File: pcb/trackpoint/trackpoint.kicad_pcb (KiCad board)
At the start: 2 copper layers, 45 x 135.9 mm, 5 parts, among them SW1 SW_RESET, SW3 SW_RESET, U1 ProMicro, U2 trackpoint_R61, U3 mouse_wheel

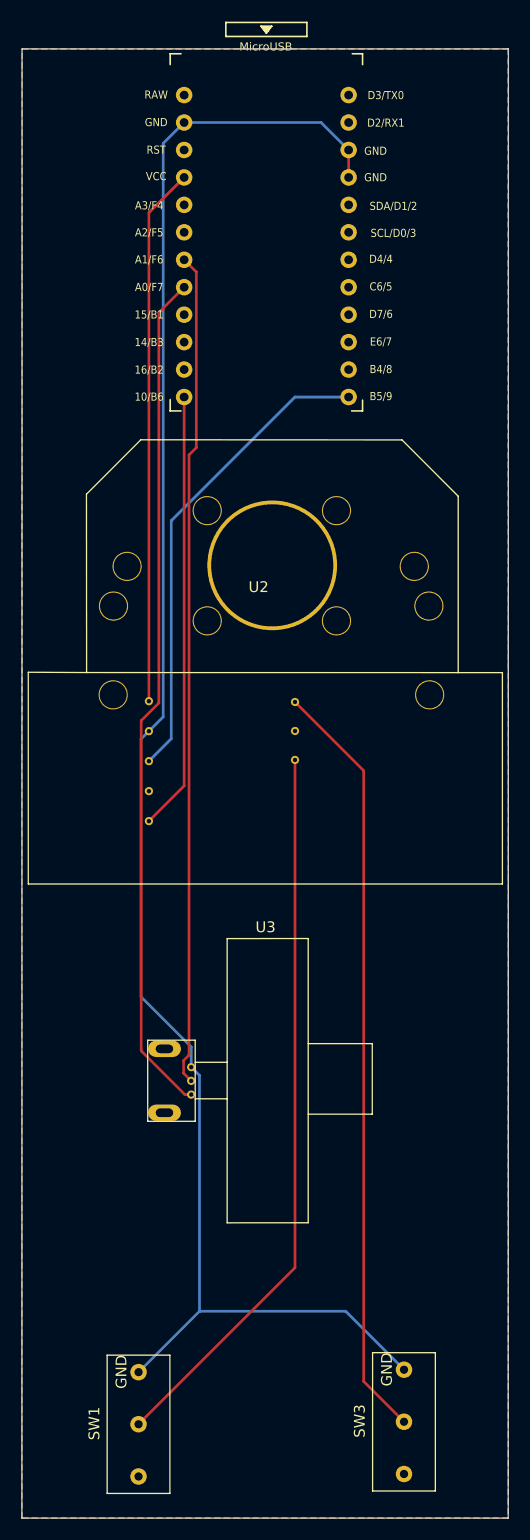
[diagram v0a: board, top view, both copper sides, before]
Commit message: keyboard settings and added arrows_R
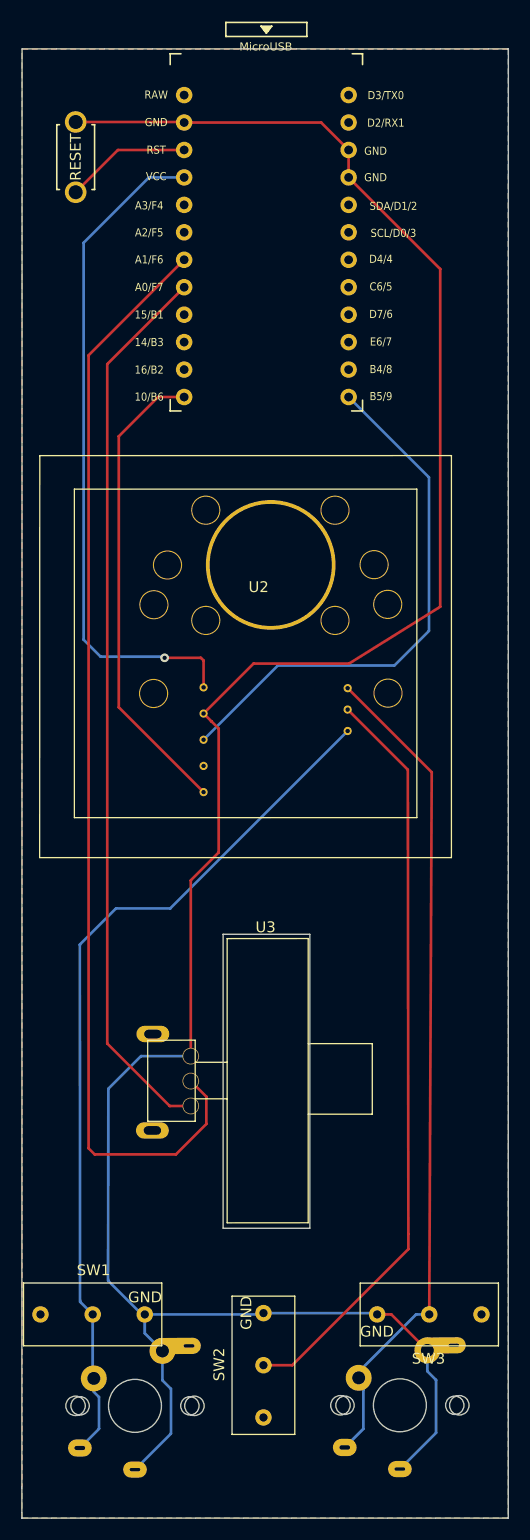
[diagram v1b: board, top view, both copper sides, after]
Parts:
- added SW0: SW_RESET, gammy:ResetSW, F.Cu at (90.1, 55.5)
- added SW01: SW_Push, gammy:CherryMX_ChocV2_1u, F.Cu at (95.6, 171.0)
- added SW03: SW_Push, gammy:CherryMX_ChocV2_1u, F.Cu at (120.1, 171.0)
- added SW2: MouseClick, gammy:mouse_click, F.Cu at (107.5, 167.3)
- SW1, SW3: value SW_RESET -> MouseClick
- moved SW1 11.0 mm to (91.7, 162.6), turned to 180 degrees
- moved SW3 10.2 mm to (122.8, 162.6), turned to 0 degrees
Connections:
- net Net-(U1-Pad12) renamed CLK
- net Net-(U1-Pad13) renamed DATA
- U1 pad 22: (no net) -> Net-(SW0-Pad1)
- U2 pad 4: (no net) -> Net-(SW2-Pad1)
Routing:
- net Net-(SW2-Pad1): track 0.00 -> 70.1 mm
- net GND: track 161.8 -> 224.5 mm
- net Net-(U1-Pad18): track 77.2 -> 102.7 mm
- net Net-(SW01-Pad1): track 67.5 -> 81.0 mm
- net VCC: track 49.8 -> 62.9 mm, vias 0 -> 1
- net Net-(SW0-Pad1): track 0.00 -> 11.7 mm
- net Net-(SW03-Pad1): track 70.8 -> 77.8 mm
- net CLK: track 44.3 -> 49.7 mm
- net Net-(U1-Pad17): track 78.6 -> 83.0 mm
- net DATA: track 40.6 -> 43.7 mm
- added copper zone on F.Cu, net Net-(SW01-Pad1)
- added copper zone on B.Cu, net Net-(SW03-Pad1)
- removed copper zone on B.Cu, net (none)
- removed copper zone on F.Cu, net (none)
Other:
- outline, holes or cut-outs redrawn
